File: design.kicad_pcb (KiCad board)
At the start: 2 copper layers, 80 x 55 mm, 87 parts, among them J1 2601-3108, J10 Conn_01x04, J11 Conn_01x04, J12 Conn_01x03, J13 Conn_01x03, J14 BM04B-SRSS-TB_LF__SN_, J2 2601-3108, J3 2601-3108, J4 TYPE-C-31-M-12, J5 SKEDD-UPDI-4, J6 Conn_01x04, J7 Conn_01x04, J8 Conn_01x04, J9 Conn_01x04, U1 ATtiny1616-S, U2 AP2112K-3.3, U3 CP2105

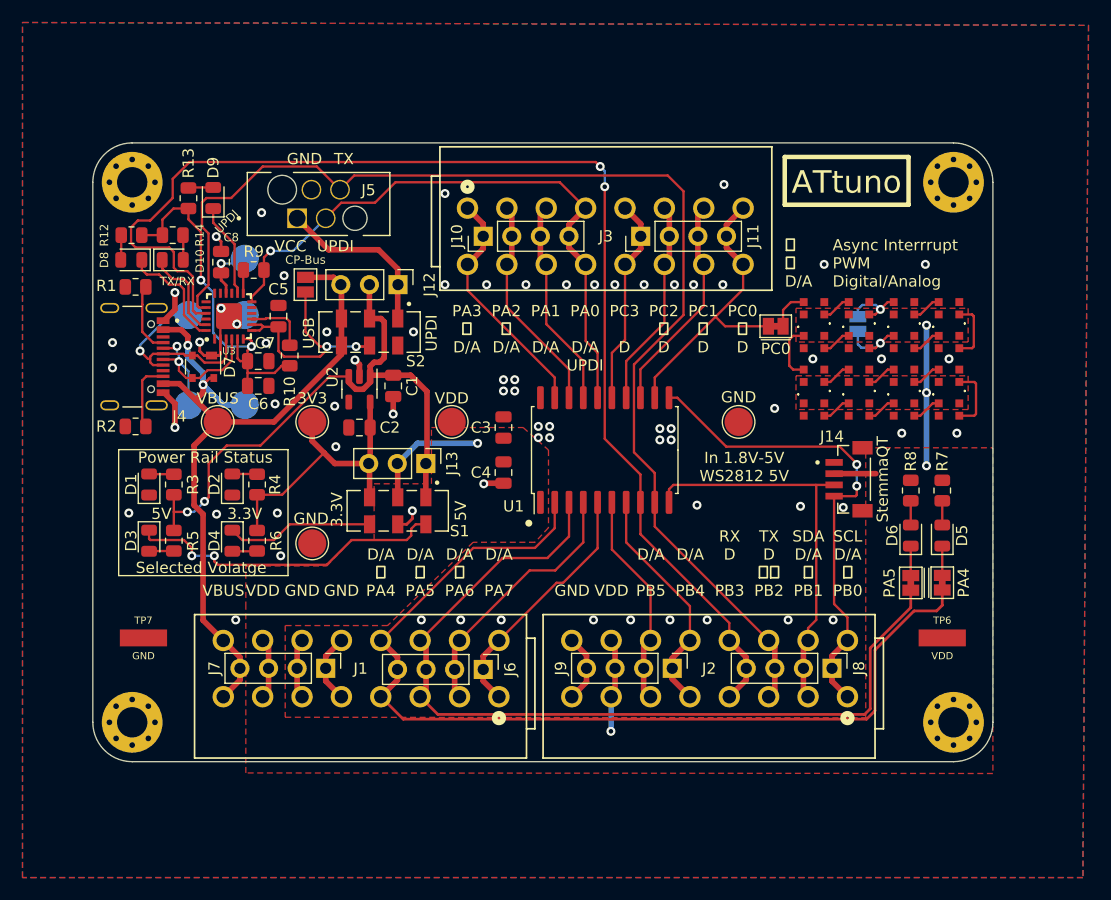
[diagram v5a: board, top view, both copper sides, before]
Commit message: Add Silkscreen update
Add information to the front.
update various information.
arrange it more neatly.
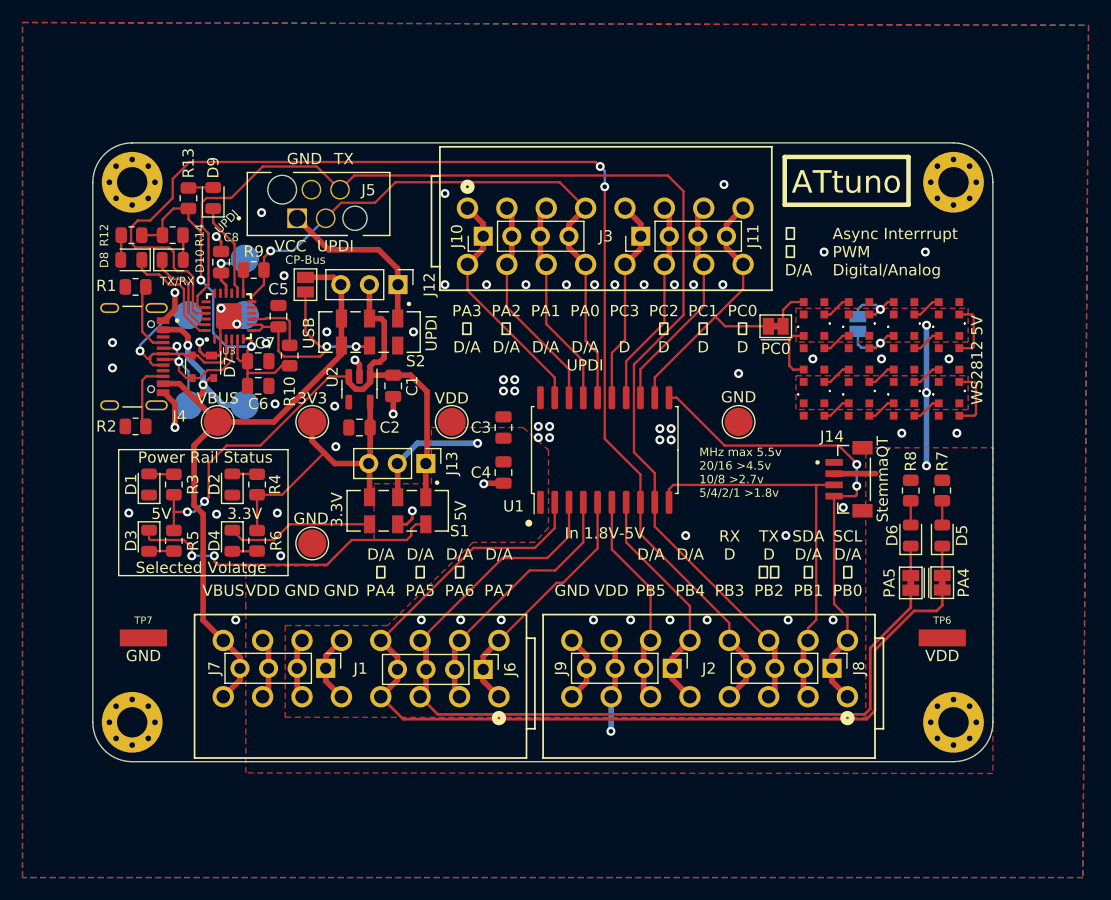
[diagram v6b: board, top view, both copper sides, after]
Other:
- board text added: "In 1.8V-5V"
- board text added: "MHz max 5.5v 20/16 >4.5v 10/8 >2.7v 5/4/2/1 >1.8v"
- board text added: "WS2812 5V"
- board text removed: "In 1.8V-5V WS2812 5V"
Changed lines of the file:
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@@
     )
     (fp_text value "GND" (at 0 1.6) (layer "F.SilkS")
-      (effects (font (size 0.64 0.64) (thickness 0.15)))
+      (effects (font (size 1 1) (thickness 0.15)))
     )
     (fp_line (start -2.35 1.05) (end 2.35 1.05) (layer "F.CrtYd") (width 0.05))
@@
     )
     (fp_text value "VDD" (at 0 1.6) (layer "F.SilkS")
-      (effects (font (size 0.64 0.64) (thickness 0.15)))
+      (effects (font (size 1 1) (thickness 0.15)))
     )
     (fp_line (start -2.35 -1.05) (end -2.35 1.05) (layer "F.CrtYd") (width 0.05))
@@
   (gr_arc (start 91 120.7) (mid 88.525126 119.674874) (end 87.5 117.2) (layer "Edge.Cuts") (width 0.05))
   (gr_arc (start 167.5 117.2) (mid 166.474874 119.674874) (end 164 120.7) (layer "Edge.Cuts") (width 0.05))
-  (gr_text "ATtiny\n416/816/1616/3216" (at 113.5 102.9) (layer "B.SilkS")
+  (gr_text "ATtiny\n416/816/1616/3216" (at 113.5 103.8) (layer "B.SilkS")
     (effects (font (size 1 1) (thickness 0.15)) (justify mirror))
   )
@@
     (effects (font (size 1 1) (thickness 0.15)))
   )
-  (gr_text "In 1.8V-5V\nWS2812 5V" (at 145.4 94.5) (layer "F.SilkS")
+  (gr_text "WS2812 5V" (at 166.1 85 90) (layer "F.SilkS")
     (effects (font (size 1 1) (thickness 0.15)))
   )
@@
     (effects (font (size 1 1) (thickness 0.15)))
   )
-  (gr_text "Async Interrrupt\nPWM\nDigital/Analog" (at 153.25 76.4) (layer "F.SilkS")
+  (gr_text "Async Interrrupt\nPWM\nDigital/Analog" (at 153.25 75.4) (layer "F.SilkS")
     (effects (font (size 1 1) (thickness 0.15)) (justify left))
   )
+  (gr_text "MHz max 5.5v\n20/16 >4.5v\n10/8 >2.7v\n5/4/2/1 >1.8v" (at 141.4 95) (layer "F.SilkS")
+    (effects (font (size 0.75 0.75) (thickness 0.12)) (justify left))
+  )
   (gr_text "Selected Volatge" (at 97.125 103.4625) (layer "F.SilkS")
     (effects (font (size 1 1) (thickness 0.15)))
   )
+  (gr_text "In 1.8V-5V" (at 133 100.4) (layer "F.SilkS")
+    (effects (font (size 1 1) (thickness 0.15)))
+  )
   (gr_text "SDA\nD/A\n〜\nPB1" (at 151.1 103.085) (layer "F.SilkS")
     (effects (font (size 1 1) (thickness 0.15)))
@@
     (effects (font (size 1 1) (thickness 0.15)))
   )
-  (gr_text "⎍\n〜\nD/A" (at 149 76.4) (layer "F.SilkS")
+  (gr_text "⎍\n〜\nD/A" (at 149 75.4) (layer "F.SilkS")
     (effects (font (size 1 1) (thickness 0.15)) (justify left))
   )
@@
   (segment (start 136.2 74) (end 136.2 75.100003) (width 0.5) (layer "F.Cu") (net 8))
   (segment (start 136.2 72.899997) (end 134.800003 71.5) (width 0.5) (layer "F.Cu") (net 8))
+  (segment (start 155.4 94.2805) (end 155.4 94.2) (width 0.21) (layer "F.Cu") (net 9))
   (segment (start 153.3875 97.1) (end 153.3875 106.6875) (width 0.21) (layer "F.Cu") (net 9))
   (segment (start 153.2 111.2976) (end 154.572599 109.925001) (width 0.5) (layer "F.Cu") (net 9))
+  (segment (start 155.4 94.2) (end 153.8 92.6) (width 0.21) (layer "F.Cu") (net 9))
+  (segment (start 143.65 92.6) (end 139.4 88.35) (width 0.21) (layer "F.Cu") (net 9))
   (segment (start 155.3 97.1) (end 155.4 97) (width 0.21) (layer "F.Cu") (net 9))
   (segment (start 153.2 112.4) (end 153.2 111.2976) (width 0.5) (layer "F.Cu") (net 9))
   (segment (start 153.3875 106.6875) (end 154.572599 107.872599) (width 0.21) (layer "F.Cu") (net 9))
   (segment (start 153.275 97.1) (end 155.3 97.1) (width 0.21) (layer "F.Cu") (net 9))
-  (segment (start 139.45 88.35) (end 138.715 88.35) (width 0.21) (layer "F.Cu") (net 9))
   (segment (start 153.2 113.552402) (end 154.572599 114.925001) (width 0.5) (layer "F.Cu") (net 9))
-  (segment (start 153.9 92.7) (end 143.8 92.7) (width 0.21) (layer "F.Cu") (net 9))
-  (segment (start 155.4 94.2) (end 153.9 92.7) (width 0.21) (layer "F.Cu") (net 9))
-  (segment (start 155.4 94.2805) (end 155.4 94.2) (width 0.21) (layer "F.Cu") (net 9))
+  (segment (start 153.8 92.6) (end 143.65 92.6) (width 0.21) (layer "F.Cu") (net 9))
   (segment (start 154.572599 107.872599) (end 154.572599 109.925001) (width 0.21) (layer "F.Cu") (net 9))
   (segment (start 153.2 112.4) (end 153.2 113.552402) (width 0.5) (layer "F.Cu") (net 9))
-  (segment (start 143.8 92.7) (end 139.45 88.35) (width 0.21) (layer "F.Cu") (net 9))
   (segment (start 155.4 97) (end 155.4 96.2) (width 0.21) (layer "F.Cu") (net 9))
+  (segment (start 139.4 88.35) (end 138.715 88.35) (width 0.21) (layer "F.Cu") (net 9))
   (via (at 155.4 94.2805) (size 0.8) (drill 0.4) (layers "F.Cu" "B.Cu") (net 9))
   (via (at 155.4 96.2) (size 0.8) (drill 0.4) (layers "F.Cu" "B.Cu") (net 9))
@@
   (via (at 140.9 78.3) (size 0.8) (drill 0.4) (layers "F.Cu" "B.Cu") (free) (net 32))
   (via (at 124 87.75) (size 0.8) (drill 0.4) (layers "F.Cu" "B.Cu") (free) (net 32))
-  (via (at 141.2 97.9) (size 0.8) (drill 0.4) (layers "F.Cu" "B.Cu") (free) (net 32))
+  (via (at 140.2 100.6) (size 0.8) (drill 0.4) (layers "F.Cu" "B.Cu") (free) (net 32))
   (via (at 138.9 91.1) (size 0.8) (drill 0.4) (layers "F.Cu" "B.Cu") (free) (net 32))
-  (via (at 152.5 76.5) (size 0.8) (drill 0.4) (layers "F.Cu" "B.Cu") (free) (net 32))
+  (via (at 152.5 75.4) (size 0.8) (drill 0.4) (layers "F.Cu" "B.Cu") (free) (net 32))
   (via (at 116 82.5) (size 0.8) (drill 0.4) (layers "F.Cu" "B.Cu") (free) (net 32))
   (via (at 128.1 91.9) (size 0.8) (drill 0.4) (layers "F.Cu" "B.Cu") (free) (net 32))
@@
   (via (at 132.1 78.3) (size 0.8) (drill 0.4) (layers "F.Cu" "B.Cu") (free) (net 32))
   (via (at 138.8 108.1) (size 0.8) (drill 0.4) (layers "F.Cu" "B.Cu") (free) (net 32))
-  (via (at 148.1 89.3) (size 0.8) (drill 0.4) (layers "F.Cu" "B.Cu") (free) (net 32))
+  (via (at 144.9 86.2) (size 0.8) (drill 0.4) (layers "F.Cu" "B.Cu") (free) (net 32))
   (via (at 154.2 98.1) (size 0.8) (drill 0.4) (layers "F.Cu" "B.Cu") (free) (net 32))
   (via (at 125 87.75) (size 0.8) (drill 0.4) (layers "F.Cu" "B.Cu") (free) (net 32))
@@
   (via (at 139.2 78.3) (size 0.8) (drill 0.4) (layers "F.Cu" "B.Cu") (free) (net 32))
   (via (at 122.25 96) (size 0.8) (drill 0.4) (layers "F.Cu" "B.Cu") (net 32))
-  (via (at 161.5 76.5) (size 0.8) (drill 0.4) (layers "F.Cu" "B.Cu") (free) (net 32))
+  (via (at 161.5 75.4) (size 0.8) (drill 0.4) (layers "F.Cu" "B.Cu") (free) (net 32))
   (via (at 94.8 91) (size 0.8) (drill 0.4) (layers "F.Cu" "B.Cu") (net 32))
   (via (at 118.8 70.2) (size 0.8) (drill 0.4) (layers "F.Cu" "B.Cu") (free) (net 32))
@@
   (via (at 94.8 79) (size 0.8) (drill 0.4) (layers "F.Cu" "B.Cu") (net 32))
   (via (at 116.7 108.1) (size 0.8) (drill 0.4) (layers "F.Cu" "B.Cu") (free) (net 32))
-  (via (at 150.4 98) (size 0.8) (drill 0.4) (layers "F.Cu" "B.Cu") (free) (net 32))
+  (via (at 149.1 100.6) (size 0.8) (drill 0.4) (layers "F.Cu" "B.Cu") (free) (net 32))
   (via (at 132 108.1) (size 0.8) (drill 0.4) (layers "F.Cu" "B.Cu") (free) (net 32))
   (via (at 142.1 108.1) (size 0.8) (drill 0.4) (layers "F.Cu" "B.Cu") (free) (net 32))

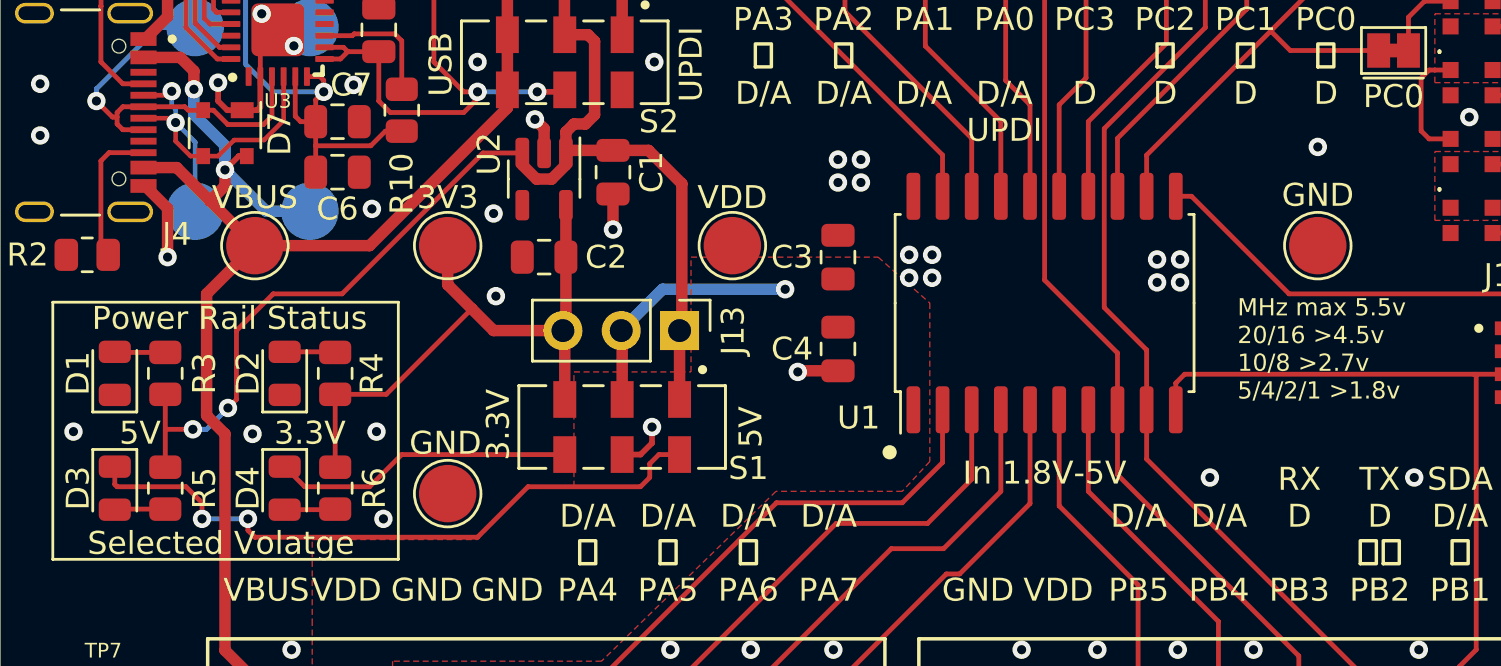
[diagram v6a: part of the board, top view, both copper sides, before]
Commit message: Updates testpoints
make them align on full intervals
add dimension marker
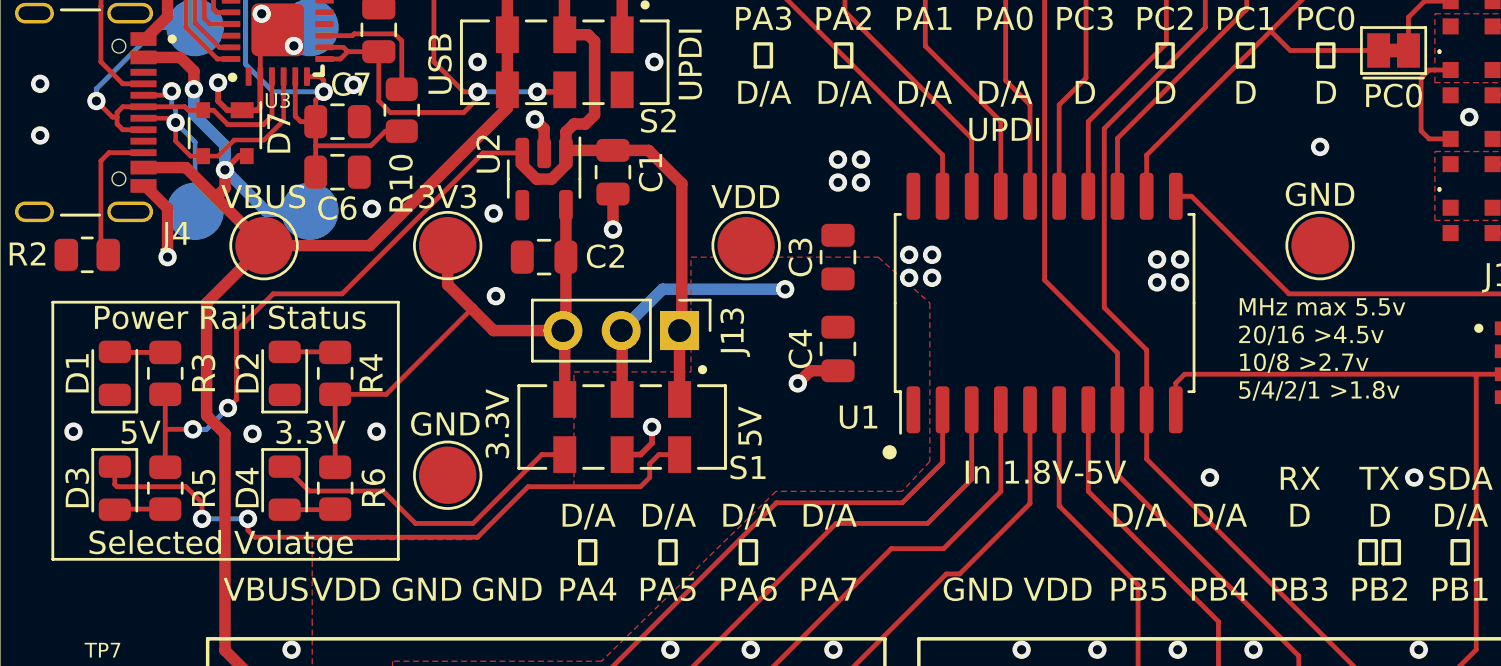
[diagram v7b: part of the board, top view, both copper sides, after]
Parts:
- moved TP1 0.80 mm to (107.0, 100.5)
- moved TP4 0.60 mm to (120.0, 90.5)
- moved TP5 0.40 mm to (99.0, 90.5)
- moved TP2 0.10 mm to (145.0, 90.5)
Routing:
- net Net-(D4-Pad1): track 13.1 -> 14.5 mm
- net GND: track 39.4 -> 39.6 mm, vias 69 -> 68

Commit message: Add ATtiny QFN
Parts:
- added U4: ATtiny1616-M, Package_DFN_QFN:VQFN-20-1EP_3x3mm_P0.4mm_EP1.7x1.7mm, F.Cu at (133.0, 93.0)
- moved JP1 1.60 mm to (148.3, 80.4)
- moved C2 0.10 mm to (111.2, 90.9)
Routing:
- net PB3: track 111.6 -> 146.2 mm, vias 2 -> 6
- net PB2: track 108.9 -> 135.4 mm, vias 0 -> 5
- net PB1: track 35.4 -> 45.6 mm
- net PA3: track 21.2 -> 27.3 mm
- net PA4: track 87.6 -> 93.0 mm
- net PA2: track 19.5 -> 24.6 mm
- net PC1: track 19.6 -> 24.6 mm
- net PA5: track 78.4 -> 83.2 mm
- net PC0: track 26.4 -> 30.7 mm
- net PA0: track 55.2 -> 59.3 mm
- net PA6: track 23.5 -> 27.6 mm
- net PC2: track 18.6 -> 22.7 mm
- net PB4: track 20.9 -> 24.6 mm
- net PA1: track 18.6 -> 22.3 mm
- net PA7: track 22.4 -> 25.9 mm
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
